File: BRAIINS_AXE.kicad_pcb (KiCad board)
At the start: 6 copper layers, 105.5 x 181.1 mm, 275 parts, among them J1 RJ45_Hanrun_HR911105A_Horizon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, J10 Connector 02x01, J2 Conn_01x06, J9 Conn_01x10, M1 Fan_4pin, M2 Fan_4pin, U10 BM1370_mode1, U11 BM1370_mode1, U12 W5500, U16 CSD95472Q5MC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

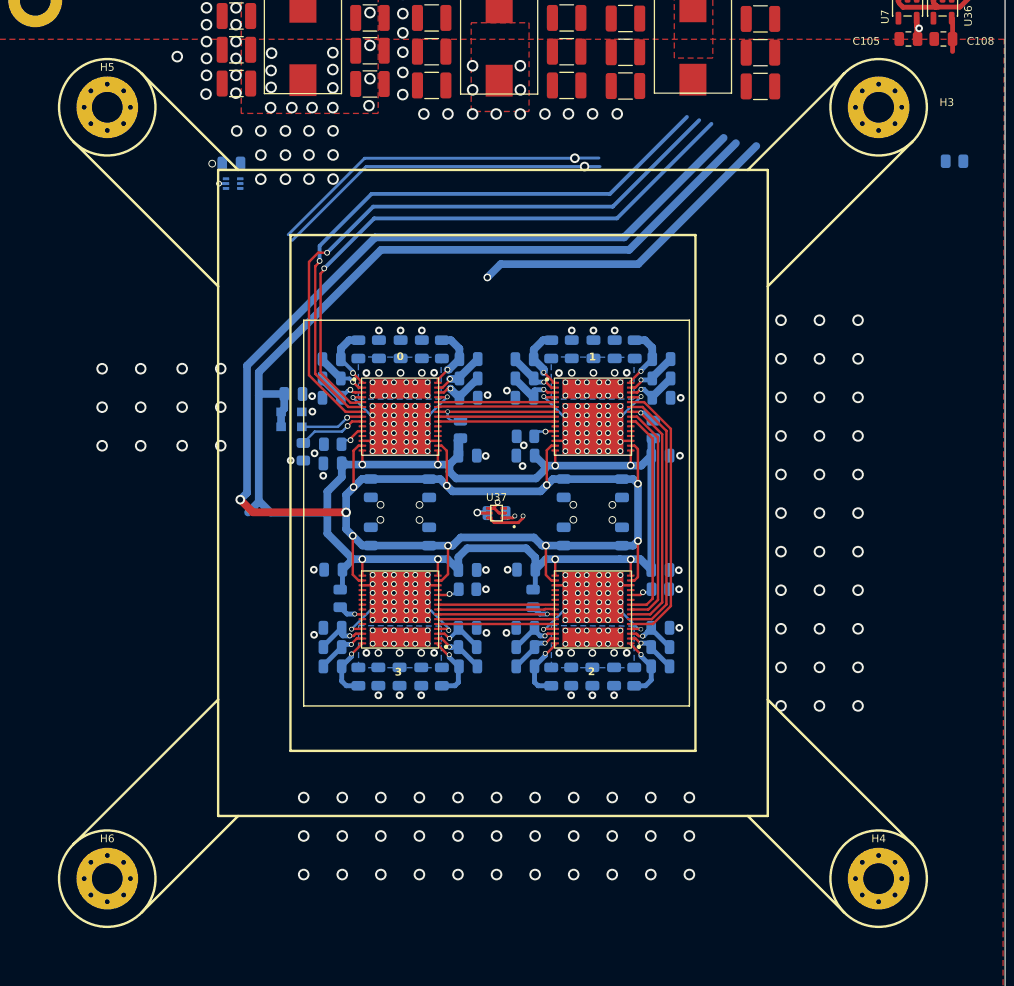
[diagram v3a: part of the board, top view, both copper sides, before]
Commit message: updated to LGA1700
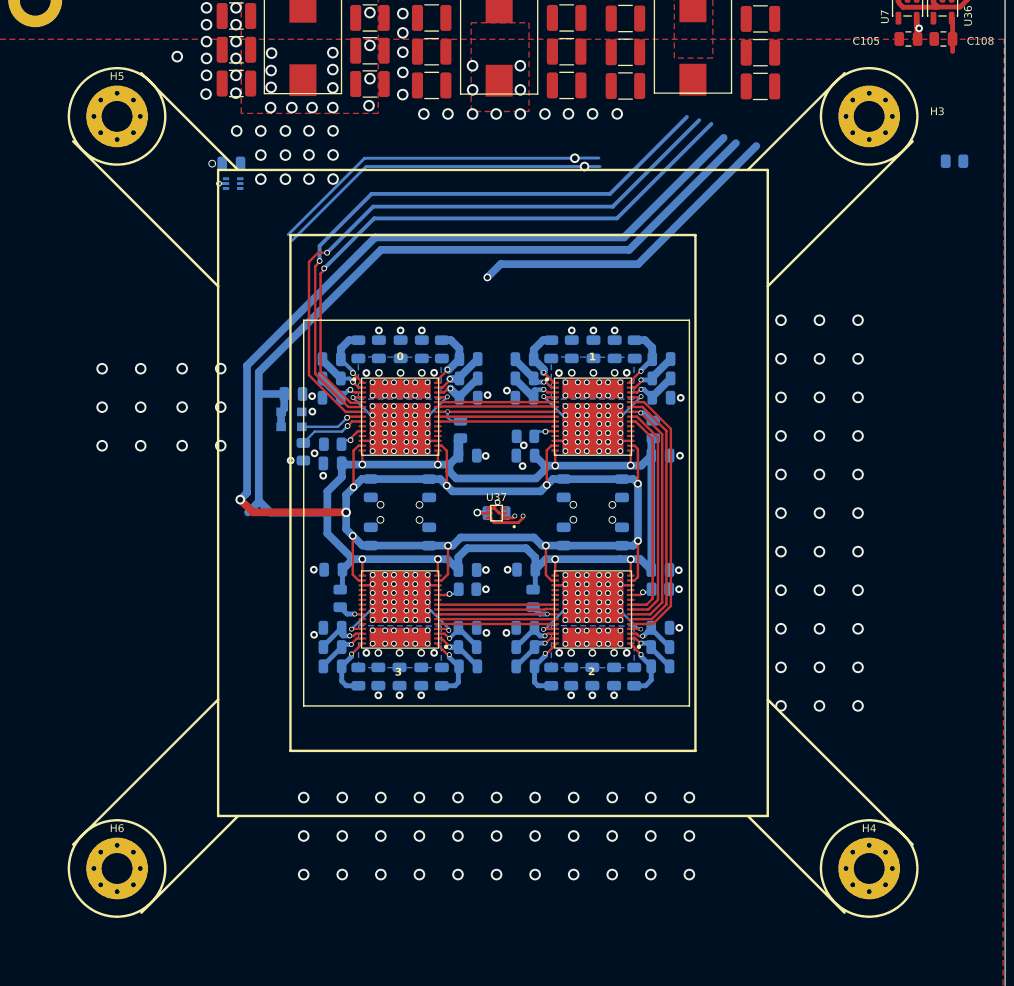
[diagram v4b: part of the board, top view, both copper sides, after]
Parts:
- moved H6 1.46 mm to (48.0, 200.0)
- moved H4 1.44 mm to (126.0, 200.0)
- moved H5 1.39 mm to (48.0, 122.0)
- moved H3 1.36 mm to (126.0, 122.0)
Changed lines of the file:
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@@
 	(footprint "MountingHole:MountingHole_3.2mm_M3_Pad_Via"
 		(layer "F.Cu")
-		(at 46.982233 201.053301)
+		(at 48 200)
 		(descr "Mounting Hole 3.2mm, M3, generated by kicad-footprint-generator mountinghole.py")
 		(tags "mountinghole M3")
@@
 	(footprint "MountingHole:MountingHole_3.2mm_M3_Pad_Via"
 		(layer "F.Cu")
-		(at 126.982233 121.053301)
+		(at 126 122)
 		(descr "Mounting Hole 3.2mm, M3, generated by kicad-footprint-generator mountinghole.py")
 		(tags "mountinghole M3")
@@
 	(footprint "MountingHole:MountingHole_3.2mm_M3_Pad_Via"
 		(layer "F.Cu")
-		(at 46.982233 121.053301)
+		(at 48 122)
 		(descr "Mounting Hole 3.2mm, M3, generated by kicad-footprint-generator mountinghole.py")
 		(tags "mountinghole M3")
@@
 	(footprint "MountingHole:MountingHole_3.2mm_M3_Pad_Via"
 		(layer "F.Cu")
-		(at 126.982233 201.053301)
+		(at 126 200)
 		(descr "Mounting Hole 3.2mm, M3, generated by kicad-footprint-generator mountinghole.py")
 		(tags "mountinghole M3")
@@
 	)
 	(gr_circle
-		(center 46.982233 121.053301)
-		(end 46.982233 126.053301)
+		(center 48 122)
+		(end 48 127)
 		(stroke
 			(width 0.25)
@@
 	)
 	(gr_circle
-		(center 46.982233 201.053301)
-		(end 46.982233 206.053301)
+		(center 48 200)
+		(end 48 205)
 		(stroke
 			(width 0.25)
@@
 	)
 	(gr_circle
-		(center 126.982233 121.053301)
-		(end 126.982233 126.053301)
+		(center 126 122)
+		(end 126 127)
 		(stroke
 			(width 0.25)
@@
 	)
 	(gr_circle
-		(center 126.982233 201.053301)
-		(end 126.982233 206.053301)
+		(center 126 200)
+		(end 126 205)
 		(stroke
 			(width 0.25)
@@
 	)
 	(gr_circle
-		(center 46.982233 121.053301)
-		(end 46.982233 123.653301)
+		(center 48 122)
+		(end 48 124.6)
 		(stroke
 			(width 0.25)
@@
 	)
 	(gr_circle
-		(center 46.982233 201.053301)
-		(end 46.982233 203.653301)
+		(center 48 200)
+		(end 48 202.6)
 		(stroke
 			(width 0.25)
@@
 	)
 	(gr_circle
-		(center 126.982233 121.053301)
-		(end 126.982233 123.653301)
+		(center 126 122)
+		(end 126 124.6)
 		(stroke
 			(width 0.25)
@@
 	)
 	(gr_circle
-		(center 126.982233 201.053301)
-		(end 126.982233 203.653301)
+		(center 126 200)
+		(end 126 202.6)
 		(stroke
 			(width 0.25)
@@
 		(layer "Dwgs.User")
 		(pts
+			(xy 48 200) (xy 126 200)
+		)
+		(height 30)
+		(orientation 0)
+		(format
+			(prefix "")
+			(suffix "")
+			(units 3)
+			(units_format 1)
+			(precision 4)
+		)
+		(style
+			(thickness 0.15)
+			(arrow_length 1.27)
+			(text_position_mode 0)
+			(arrow_direction outward)
+			(extension_height 0.58642)
+			(extension_offset 0.5)
+			(keep_text_aligned yes)
+		)
+		(gr_text "78.0000 mm"
+			(at 87 228.85 0)
+			(layer "Dwgs.User")
+			(effects
+				(font
+					(size 1 1)
+					(thickness 0.15)
+				)
+			)
+		)
+	)
+	(dimension
+		(type orthogonal)
+		(layer "Dwgs.User")
+		(pts
 			(xy 34.626977 39.05) (xy 140.090782 40.05)
 		)
@@
 			(layer "Dwgs.User")
 			(effects
+				(font
+					(size 1 1)
+					(thickness 0.15)
+				)
+			)
+		)
+	)
+	(dimension
+		(type orthogonal)
+		(layer "Dwgs.User")
+		(pts
+			(xy 126 200) (xy 126 122)
+		)
+		(height 35)
+		(orientation 1)
+		(format
+			(prefix "")
+			(suffix "")
+			(units 3)
+			(units_format 1)
+			(precision 4)
+		)
+		(style
+			(thickness 0.15)
+			(arrow_length 1.27)
+			(text_position_mode 0)
+			(arrow_direction outward)
+			(extension_height 0.58642)
+			(extension_offset 0.5)
+			(keep_text_aligned yes)
+		)
+		(gr_text "78.0000 mm"
+			(at 159.85 161 90)
+			(layer "Dwgs.User")
+			(effects

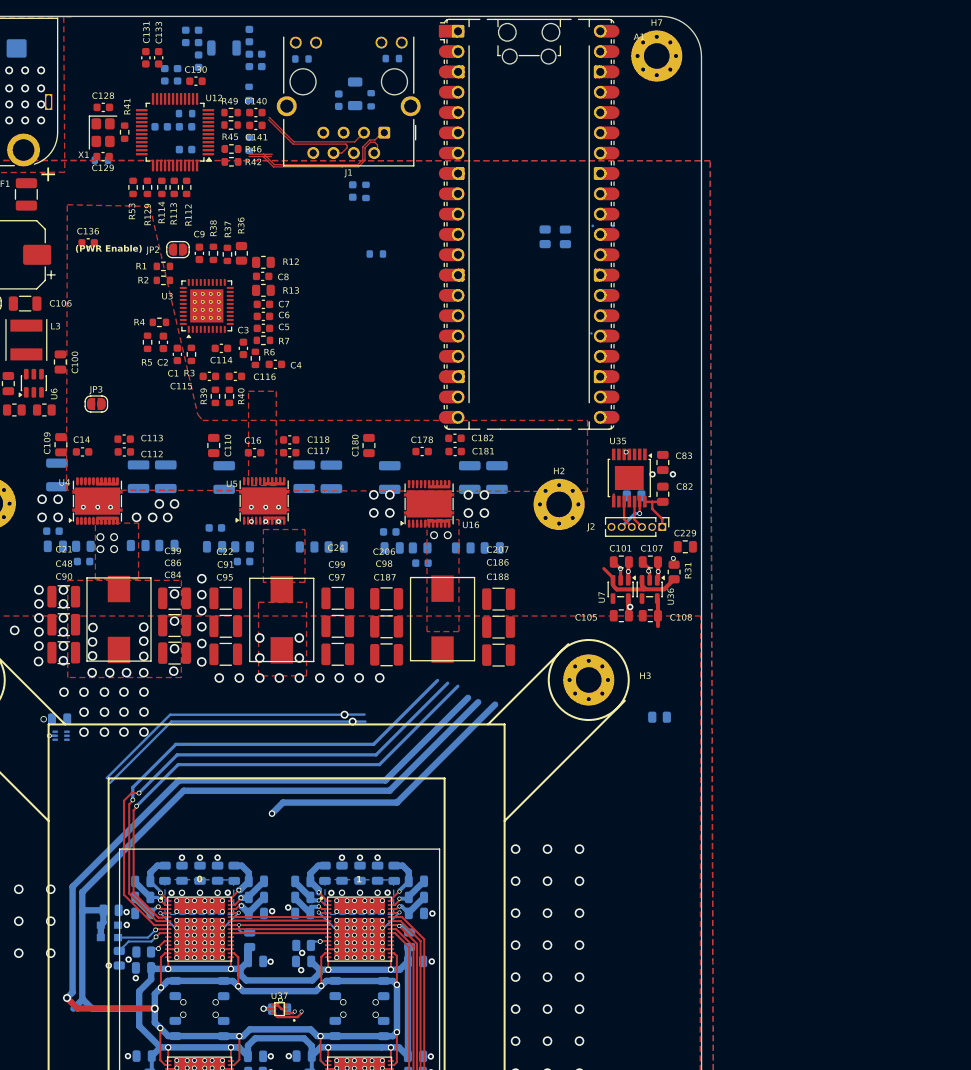
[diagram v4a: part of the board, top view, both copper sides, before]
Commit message: rp2350 connections
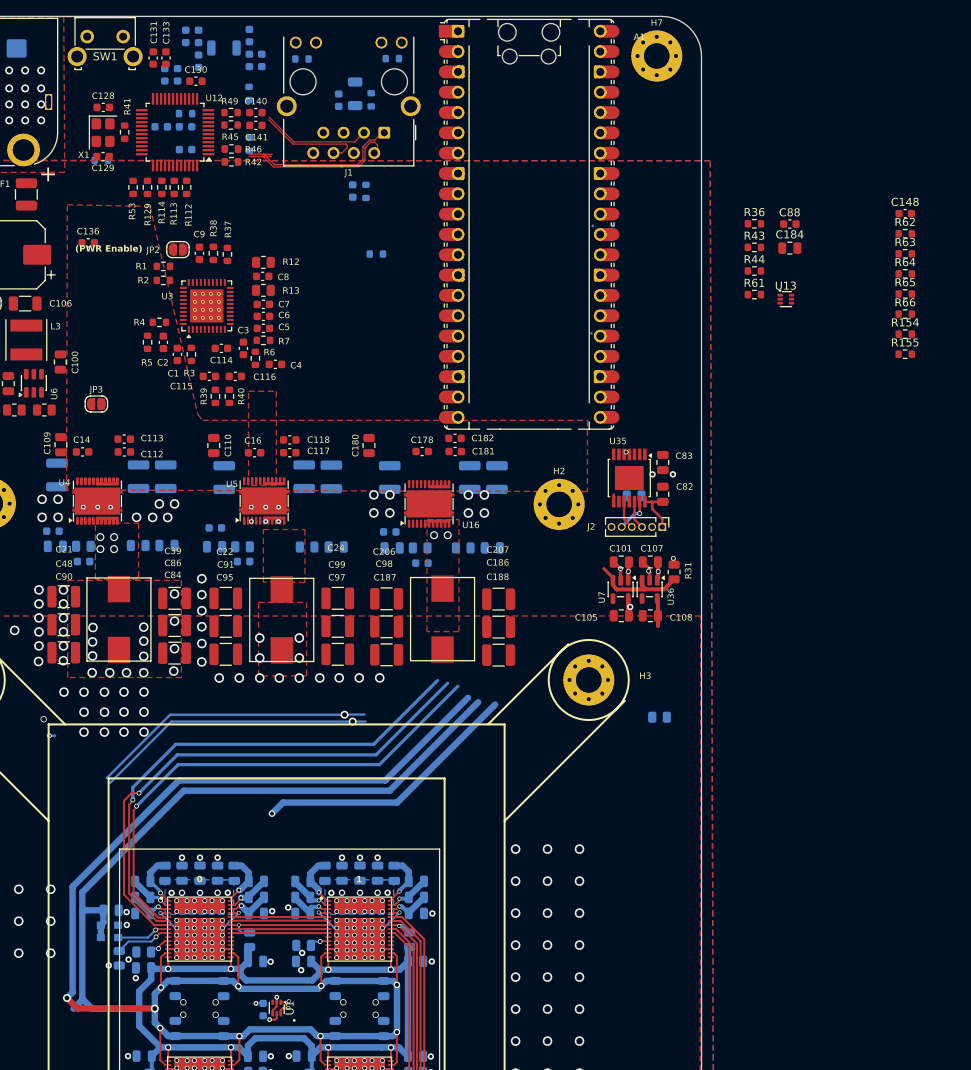
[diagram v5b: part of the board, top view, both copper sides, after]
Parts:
- removed C229: 100n/0.7mm, Capacitor_SMD:C_0805_2012Metric
- removed U37: TMP1075, myfootprints:TMP1075-DRL
- removed U38: TMP1075, Nerd8:TMP1075-DRL
- added C148: 2.2uF, Capacitor_SMD:C_0603_1608Metric, F.Cu at (165.6, 63.7)
- added C184: 10µ, Capacitor_SMD:C_0805_2012Metric, F.Cu at (151.1, 68.0)
- added R154: 33R, Resistor_SMD:R_0603_1608Metric, F.Cu at (165.6, 78.8)
- added R155: 33R, Resistor_SMD:R_0603_1608Metric, F.Cu at (165.6, 81.3)
- added R61: 10k, Resistor_SMD:R_0603_1608Metric, F.Cu at (146.7, 73.8)
- added R62: 0R, Resistor_SMD:R_0603_1608Metric, F.Cu at (165.6, 66.2)
- added R63: 0R, Resistor_SMD:R_0603_1608Metric, F.Cu at (165.6, 68.7)
- added R64: 10R, Resistor_SMD:R_0603_1608Metric, F.Cu at (165.6, 71.2)
- added R65: 2.7k, Resistor_SMD:R_0603_1608Metric, F.Cu at (165.6, 73.7)
- added R66: 2.7k, Resistor_SMD:R_0603_1608Metric, F.Cu at (165.6, 76.3)
- added SW1: SW_Omron_B3F-315x, Button_Switch_THT:SW_SPST_Omron_B3F-315x_Angled, F.Cu at (63.3, 41.6)
- added U1: TMP102xxDRL, Package_TO_SOT_SMD:SOT-563, F.Cu at (87.0, 163.0)
- added U13: TMP102xxDRL, Package_TO_SOT_SMD:SOT-563, F.Cu at (150.6, 74.4)
- C87: footprint Capacitor_SMD:C_0805_2012Metric -> Capacitor_SMD:C_0603_1608Metric
- C88: footprint Capacitor_SMD:C_0805_2012Metric -> Capacitor_SMD:C_0603_1608Metric; moved to F.Cu
- J9: value Conn_01x10 -> DISP
- R36: footprint Resistor_SMD:R_0805_2012Metric -> Resistor_SMD:R_0603_1608Metric
- R43, R44: footprint Resistor_SMD:R_0805_2012Metric -> Resistor_SMD:R_0603_1608Metric; moved to F.Cu
- moved C88 117.0 mm to (151.1, 65.0)
- moved R36 64.2 mm to (146.7, 65.0), turned to 0 degrees
- moved C87 44.3 mm to (85.3, 163.2), turned to 90 degrees
- moved R43 26.2 mm to (146.7, 67.9), turned to 0 degrees
- moved R44 24.0 mm to (146.7, 70.9), turned to 0 degrees
- moved C133 0.91 mm to (73.2, 44.2)
- moved C131 0.91 mm to (71.5, 44.2)
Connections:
- A1 pad 1: unconnected-(A1-GPIO0-Pad1) -> Net-(A1-GPIO0)
- A1 pad 10: unconnected-(A1-GPIO7-Pad10) -> /controller/DISP_SCL
- A1 pad 13: Net-(A1-GND-Pad13) -> GND
- A1 pad 18: Net-(A1-GND-Pad13) -> GND
- A1 pad 2: unconnected-(A1-GPIO1-Pad2) -> Net-(A1-GPIO1)
- A1 pad 21: unconnected-(A1-GPIO16-Pad21) -> /controller/W5500_MISO
- A1 pad 22: unconnected-(A1-GPIO17-Pad22) -> /controller/W5500_CSN
- A1 pad 23: Net-(A1-GND-Pad13) -> GND
- A1 pad 24: unconnected-(A1-GPIO18-Pad24) -> Net-(A1-GPIO18)
- A1 pad 25: unconnected-(A1-GPIO19-Pad25) -> Net-(A1-GPIO19)
- A1 pad 26: unconnected-(A1-GPIO20-Pad26) -> /controller/SDA
- A1 pad 27: unconnected-(A1-GPIO21-Pad27) -> /controller/SCL
- A1 pad 28: Net-(A1-GND-Pad13) -> GND
- A1 pad 29: unconnected-(A1-GPIO22-Pad29) -> /controller/W5500_INT_N
- A1 pad 3: Net-(A1-GND-Pad13) -> GND
- A1 pad 30: unconnected-(A1-RUN-Pad30) -> /controller/RUN
- A1 pad 31: unconnected-(A1-GPIO26_ADC0-Pad31) -> /controller/W5500_RST_N
- A1 pad 33: unconnected-(A1-AGND-Pad33) -> GND
- A1 pad 35: unconnected-(A1-ADC_VREF-Pad35) -> Net-(A1-ADC_VREF)
- A1 pad 36: unconnected-(A1-3V3-Pad36) -> 3V3
- A1 pad 38: Net-(A1-GND-Pad13) -> GND
- A1 pad 4: unconnected-(A1-GPIO2-Pad4) -> /BM1370/RESET
- A1 pad 6: unconnected-(A1-GPIO4-Pad6) -> /BM1370/TXD
- A1 pad 7: unconnected-(A1-GPIO5-Pad7) -> /BM1370/RXD
- A1 pad 8: Net-(A1-GND-Pad13) -> GND
- A1 pad 9: unconnected-(A1-GPIO6-Pad9) -> /controller/DISP_SDA
- J9 pad 1: unconnected-(J9-Pin_1-Pad1) -> /controller/DISP_SDA
- J9 pad 10: unconnected-(J9-Pin_10-Pad10) -> GND
- J9 pad 2: unconnected-(J9-Pin_2-Pad2) -> /controller/DISP_SCL
- J9 pad 9: unconnected-(J9-Pin_9-Pad9) -> 3V3
- U30 pad 19: /BM1370/TXD -> unconnected-(U30-GPIO17-Pad19)
- U30 pad 2: /BM1370/RESET -> unconnected-(U30-GPIO1-Pad2)
- U30 pad 20: /BM1370/RXD -> unconnected-(U30-GPIO18-Pad20)
- U30 pad 21: /controller/SDA -> unconnected-(U30-GPIO44-Pad21)
- U30 pad 22: /controller/SCL -> unconnected-(U30-GPIO43-Pad22)
- U30 pad 5: /Power/PWR_EN -> unconnected-(U30-GPIO10-Pad5)
- U30 pad 6: /Power/VR_RDY -> unconnected-(U30-GPIO11-Pad6)
- U30 pad 8: /Power/LDO_EN -> unconnected-(U30-GPIO13-Pad8)
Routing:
- net /controller/SDA: track 80.1 -> 78.3 mm
- net /controller/SCL: track 78.2 -> 76.4 mm
- net +3V3: track 67.2 -> 68.3 mm
- net GND: track 76.8 -> 77.1 mm, vias 294 -> 295

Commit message: fans
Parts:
- removed C102, C103, C96: 100n/0.7mm, Capacitor_SMD:C_0603_1608Metric
- removed U32: EMC2302-1, Package_SO:MSOP-10_3x3mm_P0.5mm
- removed U33: TXU0102-DCU, Package_SO:VSSOP-8_2.3x2mm_P0.5mm
- added C149: 68nF/50V, Capacitor_SMD:C_0603_1608Metric, F.Cu at (19.2, 64.7)
- added C150: 68nF/50V, Capacitor_SMD:C_0603_1608Metric, F.Cu at (19.2, 67.2)
- added D3: STPS1H100A, Diode_SMD:D_SMA, F.Cu at (13.2, 65.7)
- added D4: STPS1H100A, Diode_SMD:D_SMA, F.Cu at (13.2, 70.2)
- added D5: STPS1H100A, Diode_SMD:D_SMA, F.Cu at (13.2, 74.8)
- added Q1: BSS138, Package_TO_SOT_SMD:SOT-23, F.Cu at (19.6, 78.2)
- added Q2: BSS138, Package_TO_SOT_SMD:SOT-23, F.Cu at (19.6, 82.6)
- added R67: 0R, Resistor_SMD:R_0603_1608Metric, F.Cu at (19.2, 69.7)
- added R68: 100R, Resistor_SMD:R_0603_1608Metric, F.Cu at (19.2, 72.2)
- added R71: 100R, Resistor_SMD:R_0603_1608Metric, F.Cu at (19.2, 74.7)
- added R72: NC, Resistor_SMD:R_0603_1608Metric, F.Cu at (23.2, 64.7)
- added R73: 0R, Resistor_SMD:R_0603_1608Metric, F.Cu at (23.2, 67.2)
- added R74: 10k, Resistor_SMD:R_0603_1608Metric, F.Cu at (23.2, 69.7)
- added R75: 10k, Resistor_SMD:R_0603_1608Metric, F.Cu at (23.2, 72.2)
- added R76: 0R, Resistor_SMD:R_0603_1608Metric, F.Cu at (23.2, 74.7)
- added R77: 0R, Resistor_SMD:R_0603_1608Metric, F.Cu at (27.2, 64.7)
- added R78: NC, Resistor_SMD:R_0603_1608Metric, F.Cu at (27.2, 67.2)
- added R79: 0R, Resistor_SMD:R_0603_1608Metric, F.Cu at (27.2, 69.7)
- moved R36 64.4 mm to (82.5, 68.8), turned to -90 degrees
- moved M1 4.25 mm to (38.1, 69.5)
- moved C190 0.67 mm to (54.5, 68.8)
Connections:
- net /controller/TACHO1 renamed Net-(D4-K)
- net /controller/TACHO2 renamed Net-(D3-K)
- A1 pad 11: unconnected-(A1-GPIO8-Pad11) -> /controller/RP_PWM1
- A1 pad 12: unconnected-(A1-GPIO9-Pad12) -> /controller/RP_PWM2
- A1 pad 32: unconnected-(A1-GPIO27_ADC1-Pad32) -> /controller/RP_TACHO1
- A1 pad 34: unconnected-(A1-GPIO28_ADC2-Pad34) -> /controller/RP_TACHO2
- A1 pad 5: unconnected-(A1-GPIO3-Pad5) -> Net-(A1-GPIO3)
